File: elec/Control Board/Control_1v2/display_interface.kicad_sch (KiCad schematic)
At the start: 15 parts, among them J35 Conn_02x05_Odd_Even, J36 Conn_02x05_Odd_Even, Q601 BSS138

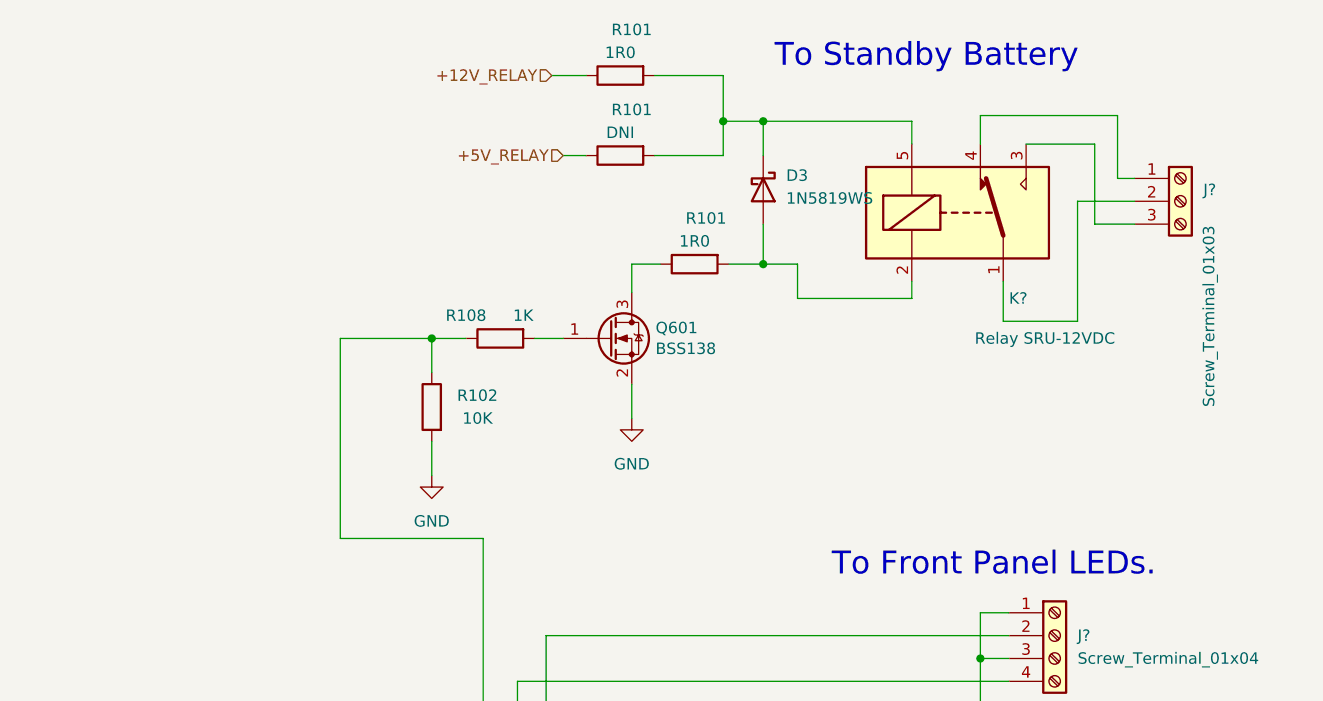
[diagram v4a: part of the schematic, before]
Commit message: Add battery relay circuit to display_interface.kicad_sch.
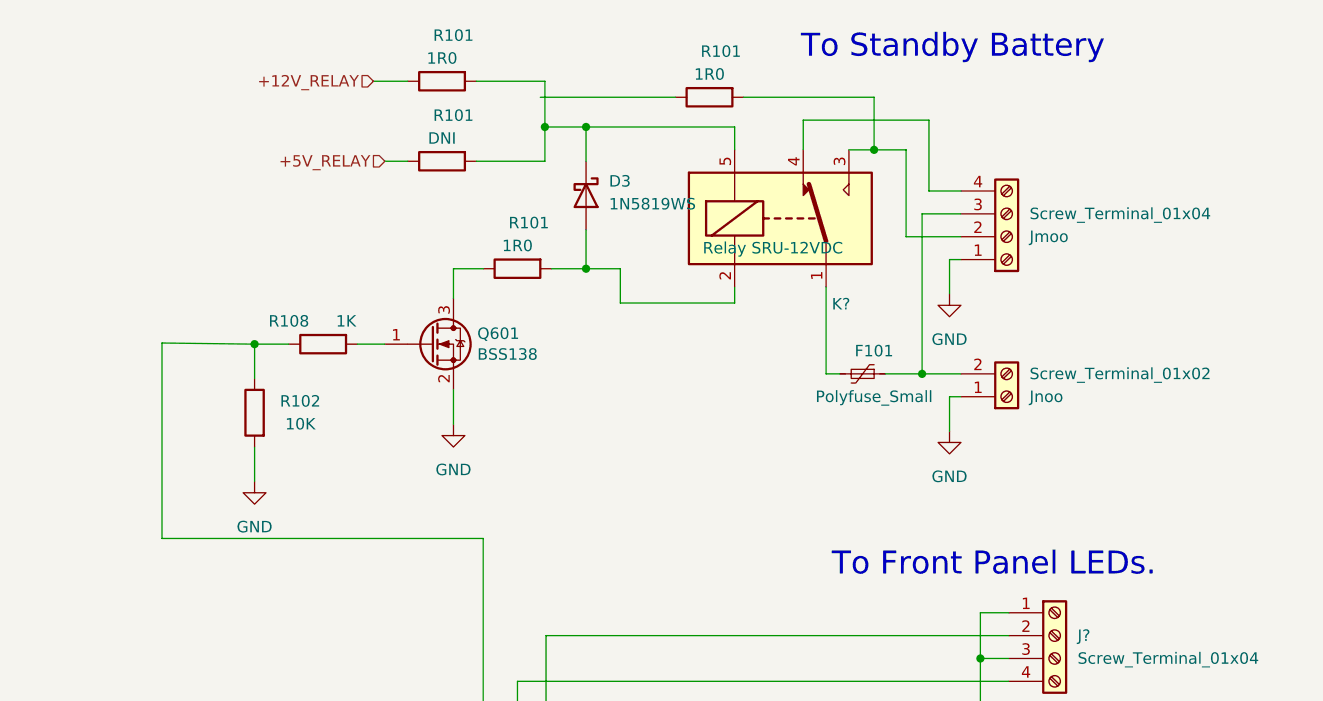
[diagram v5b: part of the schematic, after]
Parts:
- removed J?: Screw_Terminal_01x03, TerminalBlock_TE-Connectivity:TerminalBlock_TE_282834-3_1x03_P2.54mm_Horizontal, symbol Connector:Screw_Terminal_01x03
- added F101: Polyfuse_Small, Fuse:Fuse_0603_1608Metric, symbol Device:Polyfuse_Small
- added Jmoo: Screw_Terminal_01x04, TerminalBlock_TE-Connectivity:TerminalBlock_TE_282834-4_1x04_P2.54mm_Horizontal, symbol Connector:Screw_Terminal_01x04
- added Jnoo: Screw_Terminal_01x02, TerminalBlock_TE-Connectivity:TerminalBlock_TE_282834-2_1x02_P2.54mm_Horizontal, symbol Connector:Screw_Terminal_01x02
- added R101: 1R0, Resistor_SMD:R_0603_1608Metric_Pad0.98x0.95mm_HandSolder, symbol Device:R
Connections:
- net GND: now also Jmoo.1 (Pin_1), Jnoo.1 (Pin_1)
- net at K?.1: now also F101.2
- net at K?.3: now also Jmoo.2 (Pin_2), R101.2
- net at K?.4: now also Jmoo.4 (Pin_4)
- new net: F101.1, Jmoo.3 (Pin_3), Jnoo.2 (Pin_2)
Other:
- moved on the sheet: D3, K?, Q601, R101, R102, R108

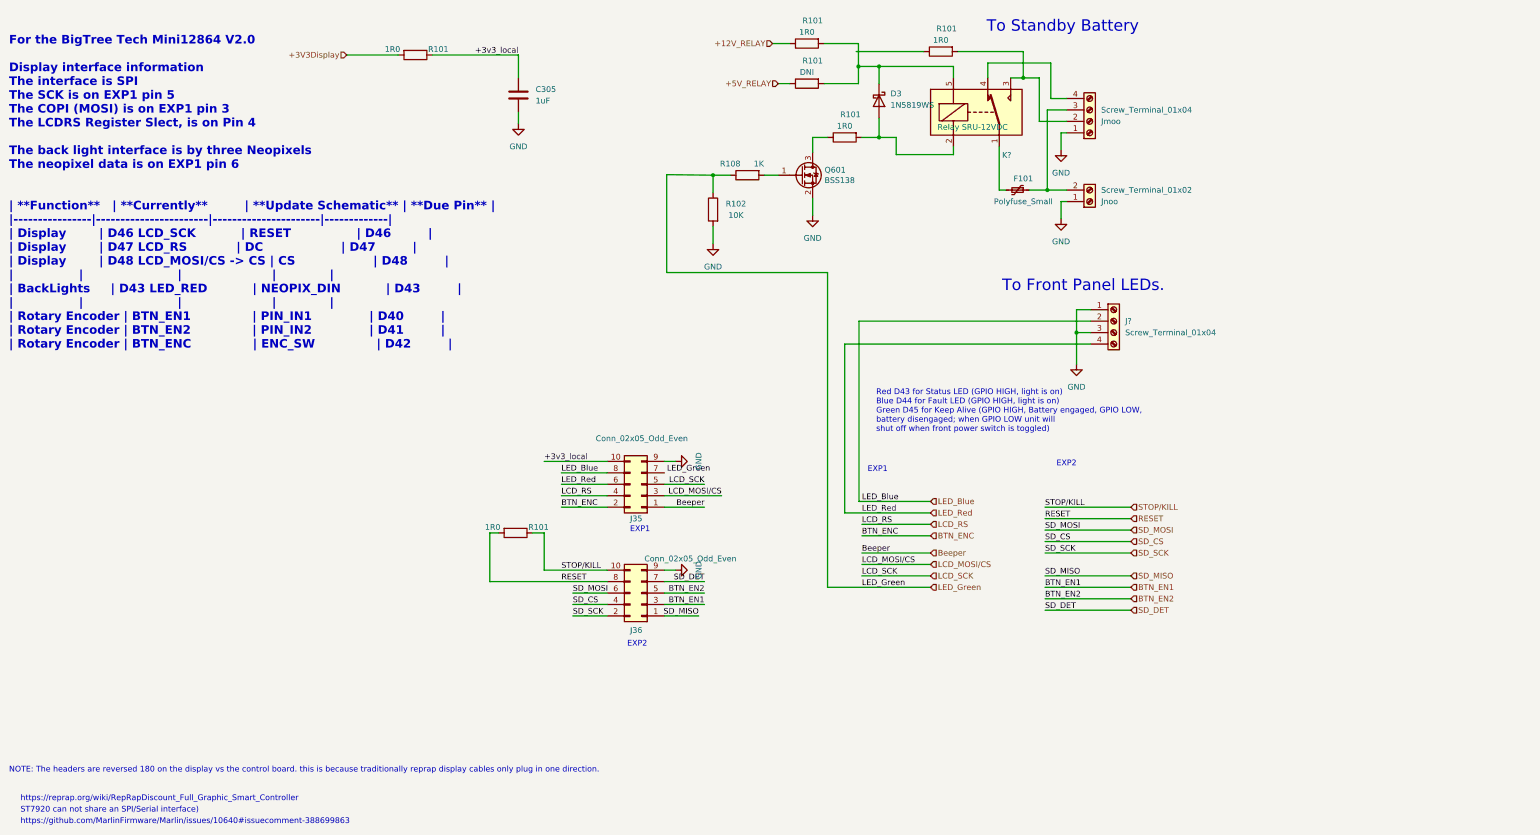
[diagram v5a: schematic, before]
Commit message: Update thermocouple page for power to new amplifier. Update Battery to screw terminal, Update O2 front panel switch and LED connections to JST XH connectors.
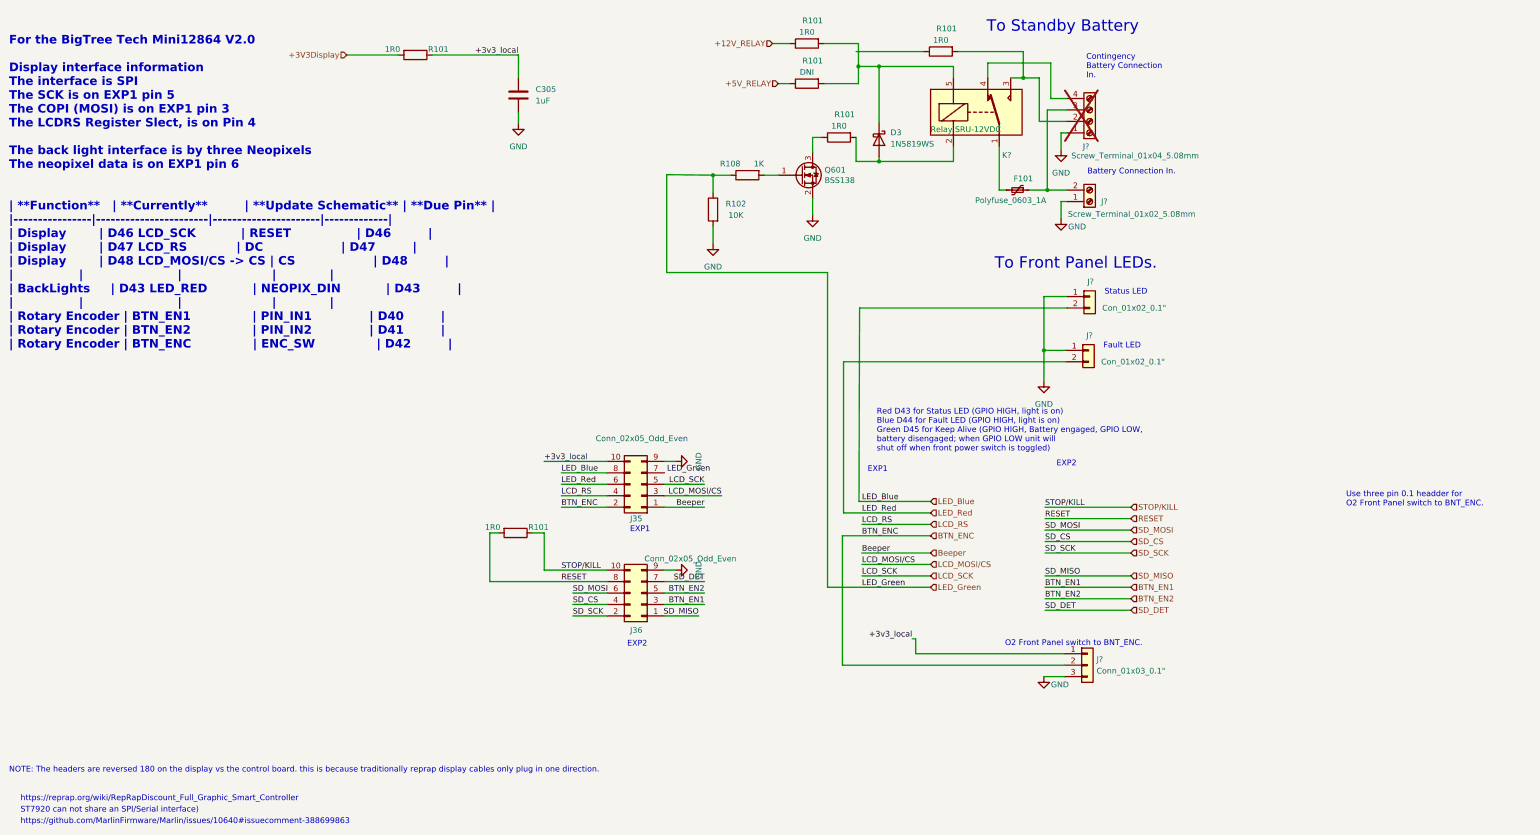
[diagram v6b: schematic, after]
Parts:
- removed J?: Screw_Terminal_01x04, TerminalBlock_TE-Connectivity:TerminalBlock_TE_282834-4_1x04_P2.54mm_Horizontal, symbol Connector:Screw_Terminal_01x04
- added J? (x2): Con_01x02_0.1", Connector_PinHeader_2.54mm:PinHeader_1x02_P2.54mm_Vertical, symbol Connector_Generic:Conn_01x02
- added J?: Conn_01x03_0.1", Connector_PinHeader_2.54mm:PinHeader_1x03_P2.54mm_Vertical, symbol Connector_Generic:Conn_01x03
- F101: value Polyfuse_Small -> Polyfuse_0603_1A
- J?: renamed from Jmoo; value Screw_Terminal_01x04 -> Screw_Terminal_01x04_5.08mm; footprint TerminalBlock_TE-Connectivity:TerminalBlock_TE_282834-4_1x04_P2.54mm_Horizontal -> TerminalBlock_Phoenix:TerminalBlock_Phoenix_MKDS-1,5-4-5.08_1x04_P5.08mm_Horizontal; Cost 0.4185 -> 1000000; Distributor 1 JLCPCB -> (none); Distributor 1 PN C474922 -> (none); MPN KF128-2.54-4P -> (none); Manufacturer Cixi Kefa Elec -> (none); now not fitted
- J?: renamed from Jnoo; value Screw_Terminal_01x02 -> Screw_Terminal_01x02_5.08mm; footprint TerminalBlock_TE-Connectivity:TerminalBlock_TE_282834-2_1x02_P2.54mm_Horizontal -> TerminalBlock_Phoenix:TerminalBlock_Phoenix_MKDS-1,5-2-5.08_1x02_P5.08mm_Horizontal; Cost 0.1920 -> 0.1551; Distributor 1 PN C474920 -> C5142622; MPN KF128-2.54-2P -> GS010B-5.08-2*02P-11-1000A(H); Manufacturer Cixi Kefa Elec -> GOOSVN
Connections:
- net +3v3_local: now also J?.1 (Pin_1)
- net BTN_ENC: now also J?.2 (Pin_2)
- net GND: now also J?.1 (Pin_1), J?.1 (Pin_1), J?.3 (Pin_3)
- net LED_Blue: now also J?.2 (Pin_2)
- net LED_Red: now also J?.2 (Pin_2)
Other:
- note added: "Battery Connection In."
- note added: "Contingency Battery Connection In."
- note added: "Fault LED"
- note added: "O2 Front Panel switch to BNT_ENC."
- note added: "Status LED"
- note added: "Use three pin 0.1 headder for O2 Front Panel switch to BNT_ENC."
- moved on the sheet: D3, R101

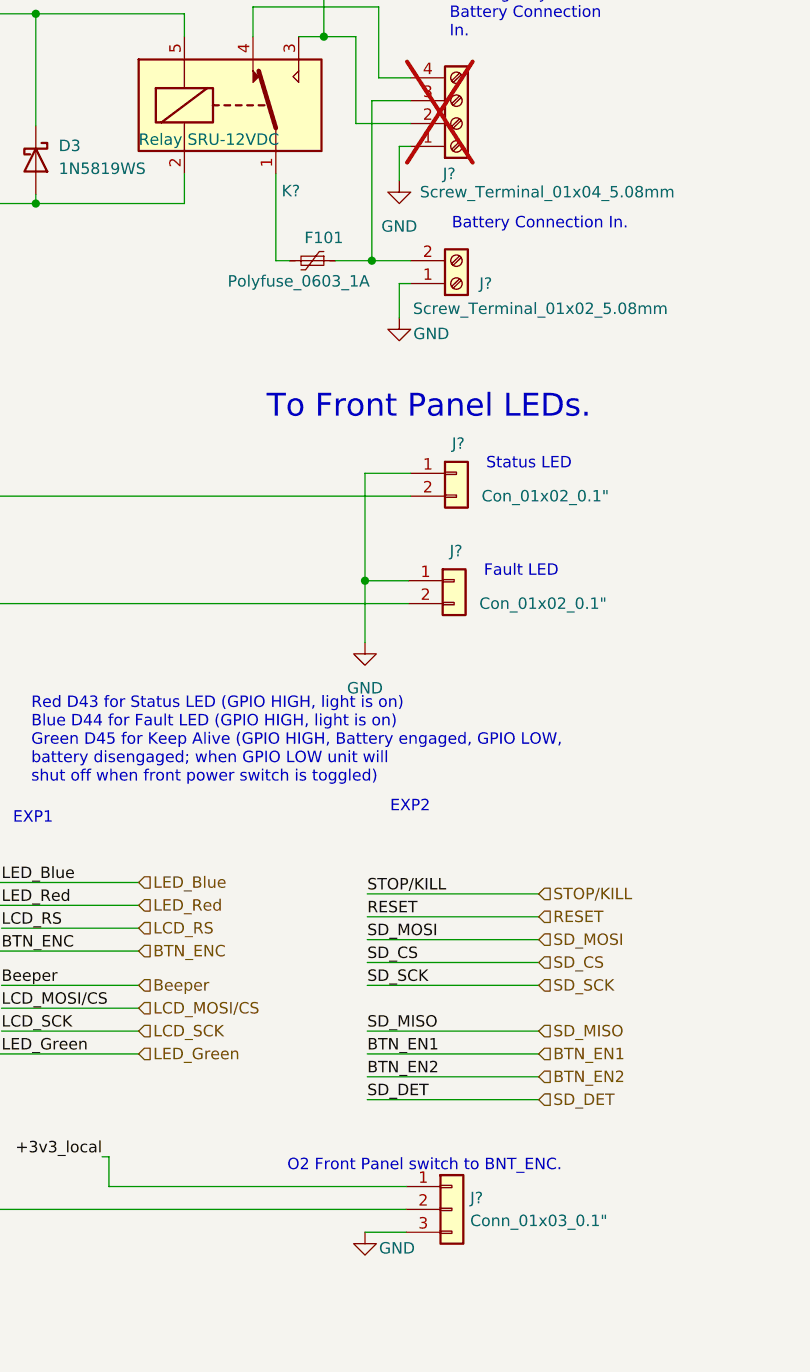
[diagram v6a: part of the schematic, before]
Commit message: Annotation of schematic for new parts in V1.2.
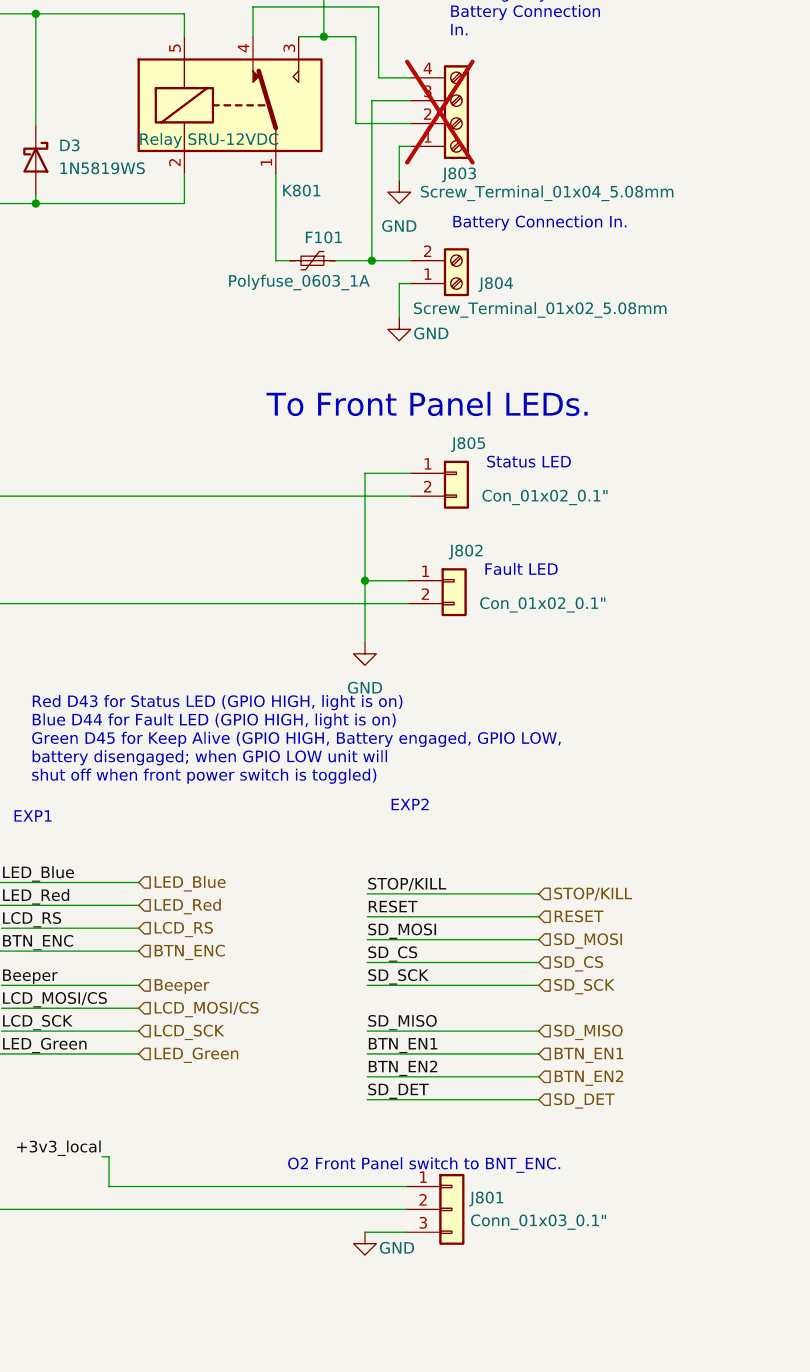
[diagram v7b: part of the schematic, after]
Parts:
- gave numbers to parts that had none: 6
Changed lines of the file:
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@@
   (symbol (lib_id "Connector_Generic:Conn_01x02") (at 258.826 76.454 0) (unit 1)
     (in_bom yes) (on_board yes) (dnp no)
-    (property "Reference" "J?" (at 258.318 73.152 0)
+    (property "Reference" "J805" (at 258.318 73.152 0)
       (effects (font (size 1.27 1.27)) (justify left))
     )
@@
       (project "Control_1v2"
         (path "/c68c9deb-8d4d-42f0-adf8-4d3022f4ee59/f2cc20dc-f81b-4e9e-a9e1-88ed6ea8264c"
-          (reference "J?") (unit 1)
+          (reference "J805") (unit 1)
         )
       )
@@
         )
         (path "/c68c9deb-8d4d-42f0-adf8-4d3022f4ee59/f2cc20dc-f81b-4e9e-a9e1-88ed6ea8264c"
-          (reference "R?") (unit 1)
+          (reference "R806") (unit 1)
         )
       )
@@
   (symbol (lib_id "Connector_Generic:Conn_01x02") (at 258.572 88.392 0) (unit 1)
     (in_bom yes) (on_board yes) (dnp no)
-    (property "Reference" "J?" (at 258.064 85.09 0)
+    (property "Reference" "J802" (at 258.064 85.09 0)
       (effects (font (size 1.27 1.27)) (justify left))
     )
@@
       (project "Control_1v2"
         (path "/c68c9deb-8d4d-42f0-adf8-4d3022f4ee59/f2cc20dc-f81b-4e9e-a9e1-88ed6ea8264c"
-          (reference "J?") (unit 1)
+          (reference "J802") (unit 1)
         )
       )
@@
   (symbol (lib_id "Relay:G5LE-1") (at 233.68 35.56 0) (unit 1)
     (in_bom yes) (on_board yes) (dnp no)
-    (property "Reference" "K?" (at 239.395 45.085 0)
+    (property "Reference" "K801" (at 239.395 45.085 0)
       (effects (font (size 1.27 1.27)) (justify left))
     )
@@
       (project "Control_1v2"
         (path "/c68c9deb-8d4d-42f0-adf8-4d3022f4ee59/f2cc20dc-f81b-4e9e-a9e1-88ed6ea8264c"
-          (reference "K?") (unit 1)
+          (reference "K801") (unit 1)
         )
       )
@@
   (symbol (lib_id "Connector:Screw_Terminal_01x04") (at 258.826 37.592 0) (mirror x) (unit 1)
     (in_bom yes) (on_board yes) (dnp yes)
-    (property "Reference" "J?" (at 257.302 43.18 0)
+    (property "Reference" "J803" (at 257.302 43.18 0)
       (effects (font (size 1.27 1.27)) (justify left))
     )
@@
       (project "Control_1v2"
         (path "/c68c9deb-8d4d-42f0-adf8-4d3022f4ee59/f2cc20dc-f81b-4e9e-a9e1-88ed6ea8264c"
-          (reference "J?") (unit 1)
+          (reference "J803") (unit 1)
         )
       )
@@
         )
         (path "/c68c9deb-8d4d-42f0-adf8-4d3022f4ee59/f2cc20dc-f81b-4e9e-a9e1-88ed6ea8264c"
-          (reference "R?") (unit 1)
+          (reference "R803") (unit 1)
         )
       )
@@
         )
         (path "/c68c9deb-8d4d-42f0-adf8-4d3022f4ee59/f2cc20dc-f81b-4e9e-a9e1-88ed6ea8264c"
-          (reference "R?") (unit 1)
+          (reference "R807") (unit 1)
         )
       )
@@
   (symbol (lib_id "Connector:Screw_Terminal_01x02") (at 258.826 55.372 0) (mirror x) (unit 1)
     (in_bom yes) (on_board yes) (dnp no)
-    (property "Reference" "J?" (at 261.366 55.372 0)
+    (property "Reference" "J804" (at 261.366 55.372 0)
       (effects (font (size 1.27 1.27)) (justify left))
     )
@@
       (project "Control_1v2"
         (path "/c68c9deb-8d4d-42f0-adf8-4d3022f4ee59/f2cc20dc-f81b-4e9e-a9e1-88ed6ea8264c"
-          (reference "J?") (unit 1)
+          (reference "J804") (unit 1)
         )
       )
@@
         )
         (path "/c68c9deb-8d4d-42f0-adf8-4d3022f4ee59/f2cc20dc-f81b-4e9e-a9e1-88ed6ea8264c"
-          (reference "R?") (unit 1)
+          (reference "R801") (unit 1)
         )
       )
@@
         )
         (path "/c68c9deb-8d4d-42f0-adf8-4d3022f4ee59/f2cc20dc-f81b-4e9e-a9e1-88ed6ea8264c"
-          (reference "Q?") (unit 1)
+          (reference "Q801") (unit 1)
         )
       )
@@
         )
         (path "/c68c9deb-8d4d-42f0-adf8-4d3022f4ee59/f2cc20dc-f81b-4e9e-a9e1-88ed6ea8264c"
-          (reference "R?") (unit 1)
+          (reference "R802") (unit 1)
         )
       )
@@
         )
         (path "/c68c9deb-8d4d-42f0-adf8-4d3022f4ee59/f2cc20dc-f81b-4e9e-a9e1-88ed6ea8264c"
-          (reference "R?") (unit 1)
+          (reference "R805") (unit 1)
         )
       )
@@
         )
         (path "/c68c9deb-8d4d-42f0-adf8-4d3022f4ee59/f2cc20dc-f81b-4e9e-a9e1-88ed6ea8264c"
-          (reference "D?") (unit 1)
+          (reference "D801") (unit 1)
         )
       )
@@
       (project "Control_1v2"
         (path "/c68c9deb-8d4d-42f0-adf8-4d3022f4ee59/f2cc20dc-f81b-4e9e-a9e1-88ed6ea8264c"
-          (reference "F?") (unit 1)
+          (reference "F801") (unit 1)
         )
       )
@@
   (symbol (lib_id "Connector_Generic:Conn_01x03") (at 258.318 158.242 0) (unit 1)
     (in_bom yes) (on_board yes) (dnp no) (fields_autoplaced)
-    (property "Reference" "J?" (at 260.35 156.972 0)
+    (property "Reference" "J801" (at 260.35 156.972 0)
       (effects (font (size 1.27 1.27)) (justify left))
     )
@@
       (project "Control_1v2"
         (path "/c68c9deb-8d4d-42f0-adf8-4d3022f4ee59/f2cc20dc-f81b-4e9e-a9e1-88ed6ea8264c"
-          (reference "J?") (unit 1)
+          (reference "J801") (unit 1)
         )
       )
@@
         )
         (path "/c68c9deb-8d4d-42f0-adf8-4d3022f4ee59/f2cc20dc-f81b-4e9e-a9e1-88ed6ea8264c"
-          (reference "R?") (unit 1)
-        )
-      )
+          (reference "R804") (unit 1)
+        )
+      )
